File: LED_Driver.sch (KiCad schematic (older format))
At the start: 0 parts

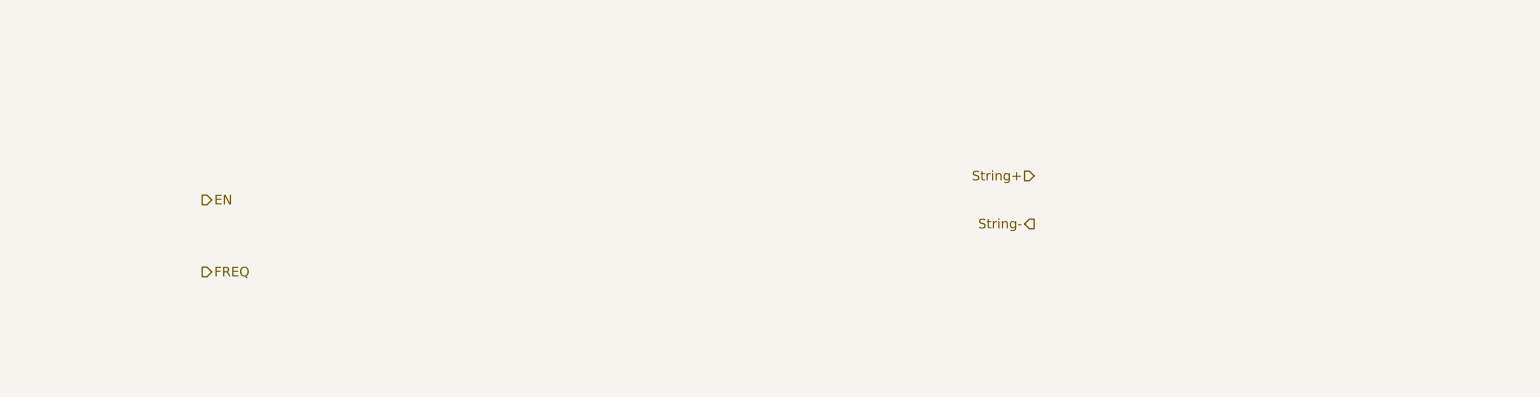
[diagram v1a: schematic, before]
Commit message: Struktur nach Arduino
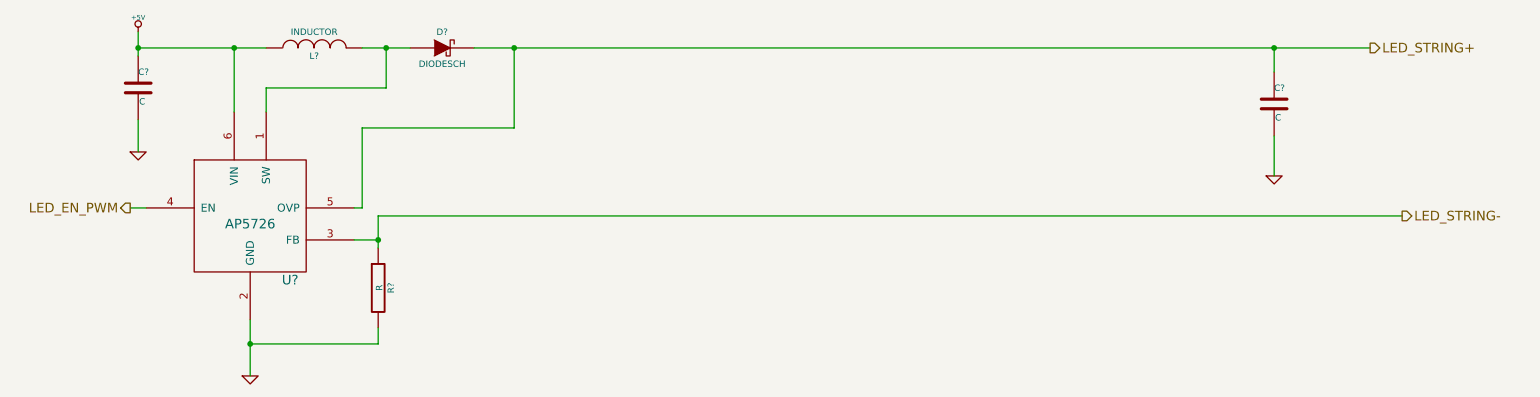
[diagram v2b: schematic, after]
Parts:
- added C? (x2): C, ~, symbol C
- added D?: DIODESCH, ~, symbol DIODESCH
- added L?: INDUCTOR, ~, symbol INDUCTOR
- added R?: R, ~, symbol R
- added U?: AP5726, symbol AP5726
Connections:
- new net: D?.1 (A), L?.2, U?.1 (SW)
- new net +5V: C?.1, L?.1, U?.6 (VIN)
- new net GND: C?.2, C?.2, R?.2, U?.2 (GND)
- new net LED_EN_PWM: U?.4 (EN)
- new net LED_STRING+: C?.1, D?.2 (K), U?.5 (OVP)
- new net LED_STRING-: R?.1, U?.3 (FB)
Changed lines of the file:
@@
 Sheet 6 9
 Title ""
-Date "4 feb 2014"
+Date "6 feb 2014"
 Rev ""
 Comp ""
@@
 Comment4 ""
 $EndDescr
-Text HLabel 2850 3300 2    60   Output ~ 0
-EN
-Text HLabel 2850 3750 2    60   Output ~ 0
-FREQ
-Text HLabel 8050 3150 0    60   Input ~ 0
-String+
-Text HLabel 8050 3450 0    60   Output ~ 0
-String-
+Text HLabel 2400 3350 0    60   Output ~ 0
+LED_EN_PWM
+Text HLabel 10150 2350 2    60   Output ~ 0
+LED_STRING+
+Text HLabel 10350 3400 2    60   Output ~ 0
+LED_STRING-
+$Comp
+L AP5726 U?
+U 1 1 52F1F3E6
+P 3150 3350
+F 0 "U?" H 3400 2900 60  0000 C CNN
+F 1 "AP5726" H 3150 3250 60  0000 C CNN
+F 2 "" H 3150 3050 60  0000 C CNN
+F 3 "" H 3150 3050 60  0000 C CNN
+	1    3150 3350
+	1    0    0    -1
+$EndComp
+Wire Wire Line
+	2500 3350 2400 3350
+$Comp
+L +5V #PWR?
+U 1 1 52F1F3FC
+P 2450 2250
+F 0 "#PWR?" H 2450 2340 20  0001 C CNN
+F 1 "+5V" H 2450 2340 30  0000 C CNN
+F 2 "" H 2450 2250 60  0000 C CNN
+F 3 "" H 2450 2250 60  0000 C CNN
+	1    2450 2250
+	1    0    0    -1
+$EndComp
+$Comp
+L GND #PWR?
+U 1 1 52F1F40B
+P 2450 3000
+F 0 "#PWR?" H 2450 3000 30  0001 C CNN
+F 1 "GND" H 2450 2930 30  0001 C CNN
+F 2 "" H 2450 3000 60  0000 C CNN
+F 3 "" H 2450 3000 60  0000 C CNN
+	1    2450 3000
+	1    0    0    -1
+$EndComp
+Wire Wire Line
+	3050 2350 3050 2750
+$Comp
+L C C?
+U 1 1 52F1F429
+P 2450 2600
+F 0 "C?" H 2450 2700 40  0000 L CNN
+F 1 "C" H 2456 2515 40  0000 L CNN
+F 2 "~" H 2488 2450 30  0000 C CNN
+F 3 "~" H 2450 2600 60  0000 C CNN
+	1    2450 2600
+	1    0    0    -1
+$EndComp
+$Comp
+L GND #PWR?
+U 1 1 52F1F45E
+P 3150 4400
+F 0 "#PWR?" H 3150 4400 30  0001 C CNN
+F 1 "GND" H 3150 4330 30  0001 C CNN
+F 2 "" H 3150 4400 60  0000 C CNN
+F 3 "" H 3150 4400 60  0000 C CNN
+	1    3150 4400
+	1    0    0    -1
+$EndComp
+Wire Wire Line
+	2450 2250 2450 2400
+Wire Wire Line
+	2450 2800 2450 3000
+Wire Wire Line
+	2450 2350 3250 2350
+Connection ~ 2450 2350
+$Comp
+L C C?
+U 1 1 52F1F477
+P 9550 2700
+F 0 "C?" H 9550 2800 40  0000 L CNN
+F 1 "C" H 9556 2615 40  0000 L CNN
+F 2 "~" H 9588 2550 30  0000 C CNN
+F 3 "~" H 9550 2700 60  0000 C CNN
+	1    9550 2700
+	1    0    0    -1
+$EndComp
+$Comp
+L INDUCTOR L?
+U 1 1 52F1F47F
+P 3550 2350
+F 0 "L?" V 3500 2350 40  0000 C CNN
+F 1 "INDUCTOR" V 3650 2350 40  0000 C CNN
+F 2 "~" H 3550 2350 60  0000 C CNN
+F 3 "~" H 3550 2350 60  0000 C CNN
+	1    3550 2350
+	0    -1   -1   0
+$EndComp
+Connection ~ 3050 2350
+Wire Wire Line
+	3850 2350 4150 2350
+Wire Wire Line
+	4000 2350 4000 2600
+Wire Wire Line
+	4000 2600 3250 2600
+Wire Wire Line
+	3250 2600 3250 2750
+$Comp
+L DIODESCH D?
+U 1 1 52F1F4A2
+P 4350 2350
+F 0 "D?" H 4350 2450 40  0000 C CNN
+F 1 "DIODESCH" H 4350 2250 40  0000 C CNN
+F 2 "~" H 4350 2350 60  0000 C CNN
+F 3 "~" H 4350 2350 60  0000 C CNN
+	1    4350 2350
+	1    0    0    -1
+$EndComp
+Connection ~ 4000 2350
+Wire Wire Line
+	9550 2350 9550 2500
+$Comp
+L GND #PWR?
+U 1 1 52F1F4F5
+P 9550 3150
+F 0 "#PWR?" H 9550 3150 30  0001 C CNN
+F 1 "GND" H 9550 3080 30  0001 C CNN
+F 2 "" H 9550 3150 60  0000 C CNN
+F 3 "" H 9550 3150 60  0000 C CNN
+	1    9550 3150
+	1    0    0    -1
+$EndComp
+Wire Wire Line
+	9550 2900 9550 3150
+Connection ~ 9550 2350
+$Comp
+L R R?
+U 1 1 52F1F53E
+P 3950 3850
+F 0 "R?" V 4030 3850 40  0000 C CNN
+F 1 "R" V 3957 3851 40  0000 C CNN
+F 2 "~" V 3880 3850 30  0000 C CNN
+F 3 "~" H 3950 3850 30  0000 C CNN
+	1    3950 3850
+	1    0    0    -1
+$EndComp
+Wire Wire Line
+	3800 3550 3950 3550
+Wire Wire Line
+	3950 3400 3950 3600
+Wire Wire Line
+	3950 4100 3950 4200
+Wire Wire Line
+	3950 4200 3150 4200
+Connection ~ 3150 4200
+Wire Wire Line
+	3150 4050 3150 4400
+Wire Wire Line
+	3950 3400 10350 3400
+Connection ~ 3950 3550
+Wire Wire Line
+	3800 3350 3850 3350
+Wire Wire Line
+	3850 3350 3850 2850
+Wire Wire Line
+	3850 2850 4800 2850
+Wire Wire Line
+	4800 2850 4800 2350
+Connection ~ 4800 2350
+Wire Wire Line
+	4550 2350 10150 2350
 $EndSCHEMATC

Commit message: Nach Einfuegen Relay-Modul
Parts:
- gave numbers to parts that had none: 6
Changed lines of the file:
@@
 Sheet 6 9
 Title ""
-Date "14 feb 2014"
+Date "17 feb 2014"
 Rev ""
 Comp ""
@@
 LED_STRING-
 $Comp
-L AP5726 U?
+L AP5726 U6
 U 1 1 52F1F3E6
 P 3150 3350
-F 0 "U?" H 3400 2900 60  0000 C CNN
+F 0 "U6" H 3400 2900 60  0000 C CNN
 F 1 "AP5726" H 3150 3250 60  0000 C CNN
 F 2 "" H 3150 3050 60  0000 C CNN
@@
 	2500 3350 2400 3350
 $Comp
-L +5V #PWR?
+L +5V #PWR29
 U 1 1 52F1F3FC
 P 2450 2250
-F 0 "#PWR?" H 2450 2340 20  0001 C CNN
+F 0 "#PWR29" H 2450 2340 20  0001 C CNN
 F 1 "+5V" H 2450 2340 30  0000 C CNN
 F 2 "" H 2450 2250 60  0000 C CNN
@@
 $EndComp
 $Comp
-L GND #PWR?
+L GND #PWR30
 U 1 1 52F1F40B
 P 2450 3000
-F 0 "#PWR?" H 2450 3000 30  0001 C CNN
+F 0 "#PWR30" H 2450 3000 30  0001 C CNN
 F 1 "GND" H 2450 2930 30  0001 C CNN
 F 2 "" H 2450 3000 60  0000 C CNN
@@
 	3050 2350 3050 2750
 $Comp
-L C C?
+L C C4
 U 1 1 52F1F429
 P 2450 2600
-F 0 "C?" H 2450 2700 40  0000 L CNN
+F 0 "C4" H 2450 2700 40  0000 L CNN
 F 1 "C" H 2456 2515 40  0000 L CNN
 F 2 "~" H 2488 2450 30  0000 C CNN
@@
 $EndComp
 $Comp
-L GND #PWR?
+L GND #PWR31
 U 1 1 52F1F45E
 P 3150 4400
-F 0 "#PWR?" H 3150 4400 30  0001 C CNN
+F 0 "#PWR31" H 3150 4400 30  0001 C CNN
 F 1 "GND" H 3150 4330 30  0001 C CNN
 F 2 "" H 3150 4400 60  0000 C CNN
@@
 Connection ~ 2450 2350
 $Comp
-L C C?
+L C C5
 U 1 1 52F1F477
 P 9550 2700
-F 0 "C?" H 9550 2800 40  0000 L CNN
+F 0 "C5" H 9550 2800 40  0000 L CNN
 F 1 "C" H 9556 2615 40  0000 L CNN
 F 2 "~" H 9588 2550 30  0000 C CNN
@@
 $EndComp
 $Comp
-L INDUCTOR L?
+L INDUCTOR L4
 U 1 1 52F1F47F
 P 3550 2350
-F 0 "L?" V 3500 2350 40  0000 C CNN
+F 0 "L4" V 3500 2350 40  0000 C CNN
 F 1 "INDUCTOR" V 3650 2350 40  0000 C CNN
 F 2 "~" H 3550 2350 60  0000 C CNN
@@
 	3250 2600 3250 2750
 $Comp
-L DIODESCH D?
+L DIODESCH D4
 U 1 1 52F1F4A2
 P 4350 2350
-F 0 "D?" H 4350 2450 40  0000 C CNN
+F 0 "D4" H 4350 2450 40  0000 C CNN
 F 1 "DIODESCH" H 4350 2250 40  0000 C CNN
 F 2 "~" H 4350 2350 60  0000 C CNN
@@
 	9550 2350 9550 2500
 $Comp
-L GND #PWR?
+L GND #PWR32
 U 1 1 52F1F4F5
 P 9550 3150
-F 0 "#PWR?" H 9550 3150 30  0001 C CNN
+F 0 "#PWR32" H 9550 3150 30  0001 C CNN
 F 1 "GND" H 9550 3080 30  0001 C CNN
 F 2 "" H 9550 3150 60  0000 C CNN
@@
 Connection ~ 9550 2350
 $Comp
-L R R?
+L R R15
 U 1 1 52F1F53E
 P 3950 3850
-F 0 "R?" V 4030 3850 40  0000 C CNN
+F 0 "R15" V 4030 3850 40  0000 C CNN
 F 1 "R" V 3957 3851 40  0000 C CNN
 F 2 "~" V 3880 3850 30  0000 C CNN

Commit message: Am Ende der 5. Woche.
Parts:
- C4, C5: value C -> 1u
- D4: value DIODESCH -> B0540WS-7
- L4: value INDUCTOR -> 22u; MFG Name (none) -> Diodes Inc; MFG Part Number (none) -> NR4012T220M
- R15: value R -> 15
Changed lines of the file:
@@
 $Descr A4 11693 8268
 encoding utf-8
-Sheet 6 9
+Sheet 5 9
 Title ""
-Date "17 feb 2014"
+Date "22 feb 2014"
 Rev ""
 Comp ""
@@
 	2500 3350 2400 3350
 $Comp
-L +5V #PWR29
+L +5V #PWR034
 U 1 1 52F1F3FC
 P 2450 2250
-F 0 "#PWR29" H 2450 2340 20  0001 C CNN
+F 0 "#PWR034" H 2450 2340 20  0001 C CNN
 F 1 "+5V" H 2450 2340 30  0000 C CNN
 F 2 "" H 2450 2250 60  0000 C CNN
@@
 $EndComp
 $Comp
-L GND #PWR30
+L GND #PWR035
 U 1 1 52F1F40B
 P 2450 3000
-F 0 "#PWR30" H 2450 3000 30  0001 C CNN
+F 0 "#PWR035" H 2450 3000 30  0001 C CNN
 F 1 "GND" H 2450 2930 30  0001 C CNN
 F 2 "" H 2450 3000 60  0000 C CNN
@@
 P 2450 2600
 F 0 "C4" H 2450 2700 40  0000 L CNN
-F 1 "C" H 2456 2515 40  0000 L CNN
+F 1 "1u" H 2456 2515 40  0000 L CNN
 F 2 "~" H 2488 2450 30  0000 C CNN
 F 3 "~" H 2450 2600 60  0000 C CNN
@@
 $EndComp
 $Comp
-L GND #PWR31
+L GND #PWR036
 U 1 1 52F1F45E
 P 3150 4400
-F 0 "#PWR31" H 3150 4400 30  0001 C CNN
+F 0 "#PWR036" H 3150 4400 30  0001 C CNN
 F 1 "GND" H 3150 4330 30  0001 C CNN
 F 2 "" H 3150 4400 60  0000 C CNN
@@
 P 9550 2700
 F 0 "C5" H 9550 2800 40  0000 L CNN
-F 1 "C" H 9556 2615 40  0000 L CNN
+F 1 "1u" H 9556 2615 40  0000 L CNN
 F 2 "~" H 9588 2550 30  0000 C CNN
 F 3 "~" H 9550 2700 60  0000 C CNN
@@
 P 3550 2350
 F 0 "L4" V 3500 2350 40  0000 C CNN
-F 1 "INDUCTOR" V 3650 2350 40  0000 C CNN
+F 1 "22u" V 3650 2350 40  0000 C CNN
 F 2 "~" H 3550 2350 60  0000 C CNN
 F 3 "~" H 3550 2350 60  0000 C CNN
+F 4 "Diodes Inc" H 3550 2350 60  0001 C CNN "MFG Name"
+F 5 "NR4012T220M" H 3550 2350 60  0001 C CNN "MFG Part Number"
 	1    3550 2350
 	0    -1   -1   0
@@
 P 4350 2350
 F 0 "D4" H 4350 2450 40  0000 C CNN
-F 1 "DIODESCH" H 4350 2250 40  0000 C CNN
+F 1 "B0540WS-7" H 4350 2250 40  0000 C CNN
 F 2 "~" H 4350 2350 60  0000 C CNN
 F 3 "~" H 4350 2350 60  0000 C CNN
@@
 	9550 2350 9550 2500
 $Comp
-L GND #PWR32
+L GND #PWR037
 U 1 1 52F1F4F5
 P 9550 3150
-F 0 "#PWR32" H 9550 3150 30  0001 C CNN
+F 0 "#PWR037" H 9550 3150 30  0001 C CNN
 F 1 "GND" H 9550 3080 30  0001 C CNN
 F 2 "" H 9550 3150 60  0000 C CNN
@@
 P 3950 3850
 F 0 "R15" V 4030 3850 40  0000 C CNN
-F 1 "R" V 3957 3851 40  0000 C CNN
+F 1 "15" V 3957 3851 40  0000 C CNN
 F 2 "~" V 3880 3850 30  0000 C CNN
 F 3 "~" H 3950 3850 30  0000 C CNN
